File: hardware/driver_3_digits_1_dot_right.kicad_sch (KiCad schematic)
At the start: 11 parts, among them U4 HV5622PG

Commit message: Update.
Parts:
- removed C10: 100nF, Capacitor_SMD:C_1206_3216Metric, symbol Device:C
- removed C9: 0.1uF, Capacitor_SMD:C_1206_3216Metric, symbol Device:C
- removed DOT1: IN-3, nixies-us:nixies-us-IN-3, symbol nixies-us:IN-3
- removed N1, N2, N3: IN-14, nixies-us:nixies-us-IN-14, symbol nixies-us:IN-14
- removed R6, R7, R8: 27K, Resistor_SMD:R_1206_3216Metric, symbol Device:R
- removed R9: 120K, Resistor_SMD:R_1206_3216Metric, symbol Device:R
- removed U4: HV5622PG, Package_QFP:PQFP-44_10x10mm_P0.8mm, symbol HV5622:HV5622PG
- added C13: 0.1uF, Capacitor_SMD:C_1206_3216Metric, symbol Device:C
- added C14: 100nF, Capacitor_SMD:C_1206_3216Metric, symbol Device:C
- added DOT2: IN-3, nixies-us:nixies-us-IN-3, symbol nixies-us:IN-3
- added N4, N5, N6: IN-14, nixies-us:nixies-us-IN-14, symbol nixies-us:IN-14
- added R15, R16, R17: 27K, Resistor_SMD:R_1206_3216Metric, symbol Device:R
- added R18: 120K, Resistor_SMD:R_1206_3216Metric, symbol Device:R
- added U5: HV5622PG, Package_QFP:PQFP-44_10x10mm_P0.8mm, symbol HV5622:HV5622PG
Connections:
- net 12V: now also C13.2, U5.30 (VDD)
- net 170V: now also C14.1, R15.1, R16.1, R17.1, R18.2
- net GND: now also C13.1, C14.2, U5.27 (~{POL}), U5.29 (VSS)
- net NOT_BL: now also U5.33 (~{BL})
- net NOT_LE: now also U5.31 (~{LE})
- net SPI_CLK: now also U5.28 (CLK)
- net SPI_SDI: now also U5.32 (DATA_IN)
- net SPI_SDO: now also U5.23 (DATA_OUT)
- new net: N4.A, R17.2
- new net: DOT2.A, R18.1
- new net: DOT2.K, U5.11 (HVOUT12)
- new net: N5.A, R16.2
- new net: N6.A, R15.2
- new net: N5.0, U5.10 (HVOUT13)
- new net: N5.1, U5.1 (HVOUT22)
- new net: N5.2, U5.2 (HVOUT21)
- new net: N5.3, U5.3 (HVOUT20)
- new net: N5.4, U5.4 (HVOUT19)
- new net: N5.5, U5.5 (HVOUT18)
- new net: N5.6, U5.6 (HVOUT17)
- new net: N5.7, U5.7 (HVOUT16)
- new net: N5.8, U5.8 (HVOUT15)
- new net: N5.9, U5.9 (HVOUT14)
- new net: N6.0, U5.21 (HVOUT2)
- new net: N6.1, U5.12 (HVOUT11)
- new net: N6.2, U5.13 (HVOUT10)
- new net: N6.3, U5.14 (HVOUT9)
- new net: N6.4, U5.15 (HVOUT8)
- new net: N6.5, U5.16 (HVOUT7)
- new net: N6.6, U5.17 (HVOUT6)
- new net: N6.7, U5.18 (HVOUT5)
- new net: N6.8, U5.19 (HVOUT4)
- new net: N6.9, U5.20 (HVOUT3)
- new net: N6.RHDP, U5.22 (HVOUT1)
- new net: N4.0, U5.44 (HVOUT23)
- new net: N4.1, U5.35 (HVOUT32)
- new net: N4.2, U5.36 (HVOUT31)
- new net: N4.3, U5.37 (HVOUT30)
- new net: N4.4, U5.38 (HVOUT29)
- new net: N4.5, U5.39 (HVOUT28)
- new net: N4.6, U5.40 (HVOUT27)
- new net: N4.7, U5.41 (HVOUT26)
- new net: N4.8, U5.42 (HVOUT25)
- new net: N4.9, U5.43 (HVOUT24)
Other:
- title: Nixie driver for three IN-14 and one IN-3 tube -> (none)

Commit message: Update.
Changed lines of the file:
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@@
 		(dnp no)
 		(property "Reference" "N4"
-			(at 121.92 105.918 0)
+			(at 121.92 146.558 0)
 			(effects
 				(font

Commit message: First routage.
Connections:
- net at DOT2.K: now also U5.1 (HVOUT22); no longer U5.11 (HVOUT12)
- net at N5.0: now also U5.11 (HVOUT12); no longer U5.10 (HVOUT13)
- net at N5.1: now also U5.2 (HVOUT21); no longer U5.1 (HVOUT22)
- net at N5.2: now also U5.3 (HVOUT20); no longer U5.2 (HVOUT21)
- net at N5.3: now also U5.4 (HVOUT19); no longer U5.3 (HVOUT20)
- net at N5.4: now also U5.5 (HVOUT18); no longer U5.4 (HVOUT19)
- net at N5.5: now also U5.6 (HVOUT17); no longer U5.5 (HVOUT18)
- net at N5.6: now also U5.7 (HVOUT16); no longer U5.6 (HVOUT17)
- net at N5.7: now also U5.8 (HVOUT15); no longer U5.7 (HVOUT16)
- net at N5.8: now also U5.9 (HVOUT14); no longer U5.8 (HVOUT15)
- net at N5.9: now also U5.10 (HVOUT13); no longer U5.9 (HVOUT14)
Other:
- moved on the sheet: N5

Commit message: Add HT psu.
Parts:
- renumbered N5 to N4, N6 to N5, N4 to N6, R15 to R17, R16 to R18, R17 to R19, R18 to R20
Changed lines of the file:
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@@
 		(dnp no)
 		(fields_autoplaced yes)
-		(property "Reference" "R17"
+		(property "Reference" "R19"
 			(at 138.43 121.92 90)
 			(effects
@@
 			(project "nixie_clock"
 				(path "/90430e5f-7049-4de8-b92d-f897c4a89819/fe830805-1f17-45c2-a3b2-c398af349661"
-					(reference "R17")
+					(reference "R19")
 					(unit 1)
 				)
@@
 		(dnp no)
 		(fields_autoplaced yes)
-		(property "Reference" "R16"
+		(property "Reference" "R18"
 			(at 138.43 39.37 90)
 			(effects
@@
 			(project "nixie_clock"
 				(path "/90430e5f-7049-4de8-b92d-f897c4a89819/fe830805-1f17-45c2-a3b2-c398af349661"
-					(reference "R16")
+					(reference "R18")
 					(unit 1)
 				)
@@
 		(dnp no)
 		(fields_autoplaced yes)
-		(property "Reference" "R15"
+		(property "Reference" "R17"
 			(at 137.16 82.55 90)
 			(effects
@@
 			(project "nixie_clock"
 				(path "/90430e5f-7049-4de8-b92d-f897c4a89819/fe830805-1f17-45c2-a3b2-c398af349661"
-					(reference "R15")
+					(reference "R17")
 					(unit 1)
 				)
@@
 		(on_board yes)
 		(dnp no)
-		(property "Reference" "N5"
+		(property "Reference" "N4"
 			(at 120.65 26.67 0)
 			(effects
@@
 			(project "nixie_clock"
 				(path "/90430e5f-7049-4de8-b92d-f897c4a89819/fe830805-1f17-45c2-a3b2-c398af349661"
-					(reference "N5")
+					(reference "N4")
 					(unit 1)
 				)
@@
 		(on_board yes)
 		(dnp no)
-		(property "Reference" "N6"
+		(property "Reference" "N5"
 			(at 120.65 107.696 0)
 			(effects
@@
 			(project "nixie_clock"
 				(path "/90430e5f-7049-4de8-b92d-f897c4a89819/fe830805-1f17-45c2-a3b2-c398af349661"
-					(reference "N6")
+					(reference "N5")
 					(unit 1)
 				)
@@
 		(on_board yes)
 		(dnp no)
-		(property "Reference" "N4"
+		(property "Reference" "N6"
 			(at 121.92 146.558 0)
 			(effects
@@
 			(project "nixie_clock"
 				(path "/90430e5f-7049-4de8-b92d-f897c4a89819/fe830805-1f17-45c2-a3b2-c398af349661"
-					(reference "N4")
+					(reference "N6")
 					(unit 1)
 				)
@@
 		(dnp no)
 		(fields_autoplaced yes)
-		(property "Reference" "R18"
+		(property "Reference" "R20"
 			(at 170.18 55.88 90)
 			(effects
@@
 			(project "nixie_clock"
 				(path "/90430e5f-7049-4de8-b92d-f897c4a89819/fe830805-1f17-45c2-a3b2-c398af349661"
-					(reference "R18")
+					(reference "R20")
 					(unit 1)
 				)

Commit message: Rename nixie's names to have the right order.
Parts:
- renumbered N6 to N4, N4 to N5, N5 to N6
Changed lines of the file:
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@@
 		(on_board yes)
 		(dnp no)
-		(property "Reference" "N4"
+		(property "Reference" "N5"
 			(at 120.65 26.67 0)
 			(effects
@@
 			(project "nixie_clock"
 				(path "/90430e5f-7049-4de8-b92d-f897c4a89819/fe830805-1f17-45c2-a3b2-c398af349661"
-					(reference "N4")
+					(reference "N5")
 					(unit 1)
 				)
@@
 		(on_board yes)
 		(dnp no)
-		(property "Reference" "N5"
+		(property "Reference" "N6"
 			(at 120.65 107.696 0)
 			(effects
@@
 			(project "nixie_clock"
 				(path "/90430e5f-7049-4de8-b92d-f897c4a89819/fe830805-1f17-45c2-a3b2-c398af349661"
-					(reference "N5")
+					(reference "N6")
 					(unit 1)
 				)
@@
 		(on_board yes)
 		(dnp no)
-		(property "Reference" "N6"
+		(property "Reference" "N4"
 			(at 121.92 146.558 0)
 			(effects
@@
 			(project "nixie_clock"
 				(path "/90430e5f-7049-4de8-b92d-f897c4a89819/fe830805-1f17-45c2-a3b2-c398af349661"
-					(reference "N6")
+					(reference "N4")
 					(unit 1)
 				)

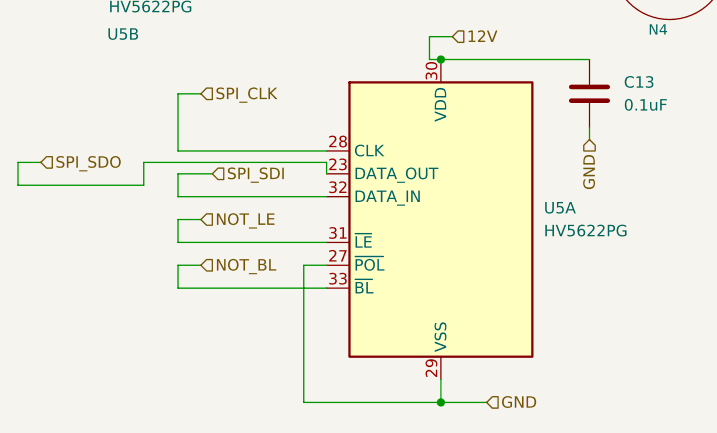
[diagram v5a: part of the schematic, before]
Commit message: Remove POLarity setup, needs 12V to be not reversed.
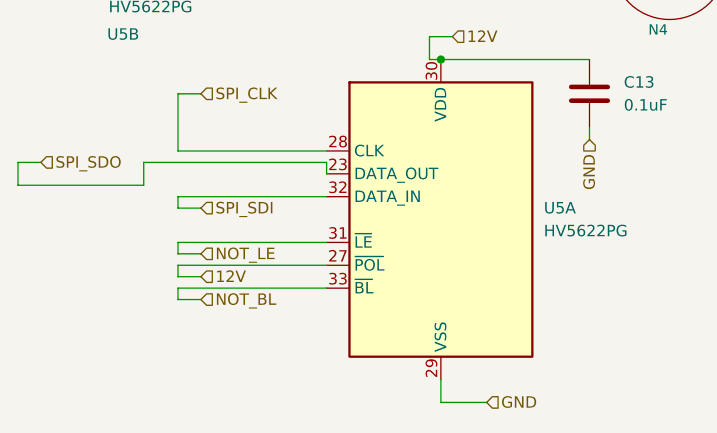
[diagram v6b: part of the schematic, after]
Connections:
- net 12V: now also U5.27 (~{POL})
- net GND: no longer U5.27 (~{POL})

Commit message: C15, C13, C9  changed to 805 form factor. Removed tracks under capacitors.
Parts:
- C13: footprint Capacitor_SMD:C_1206_3216Metric -> Resistor_SMD:R_0805_2012Metric
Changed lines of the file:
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@@
 			)
 		)
-		(property "Footprint" "Capacitor_SMD:C_1206_3216Metric"
+		(property "Footprint" "Resistor_SMD:R_0805_2012Metric"
 			(at 113.3348 149.86 0)
 			(effects

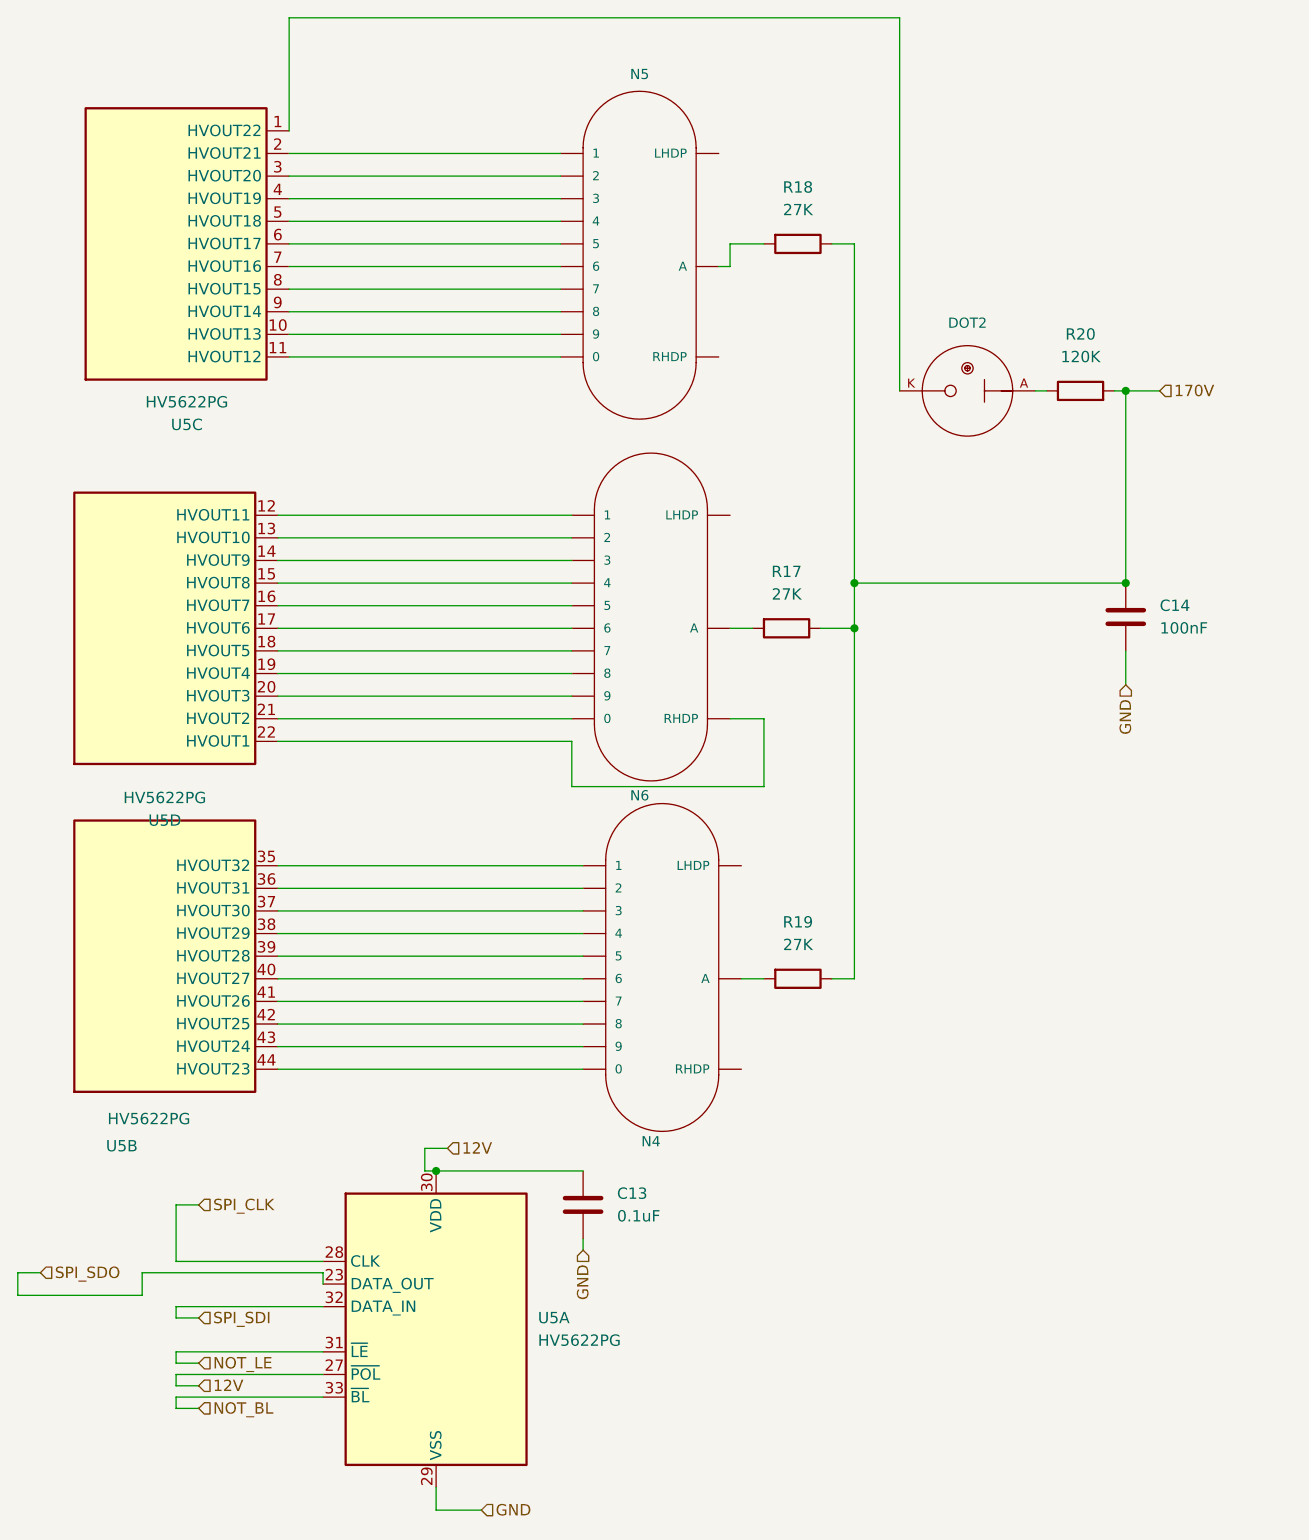
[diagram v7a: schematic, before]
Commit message: Rework  3.3v power supply (fix error on fb loop). Put 1206 back on HV part.
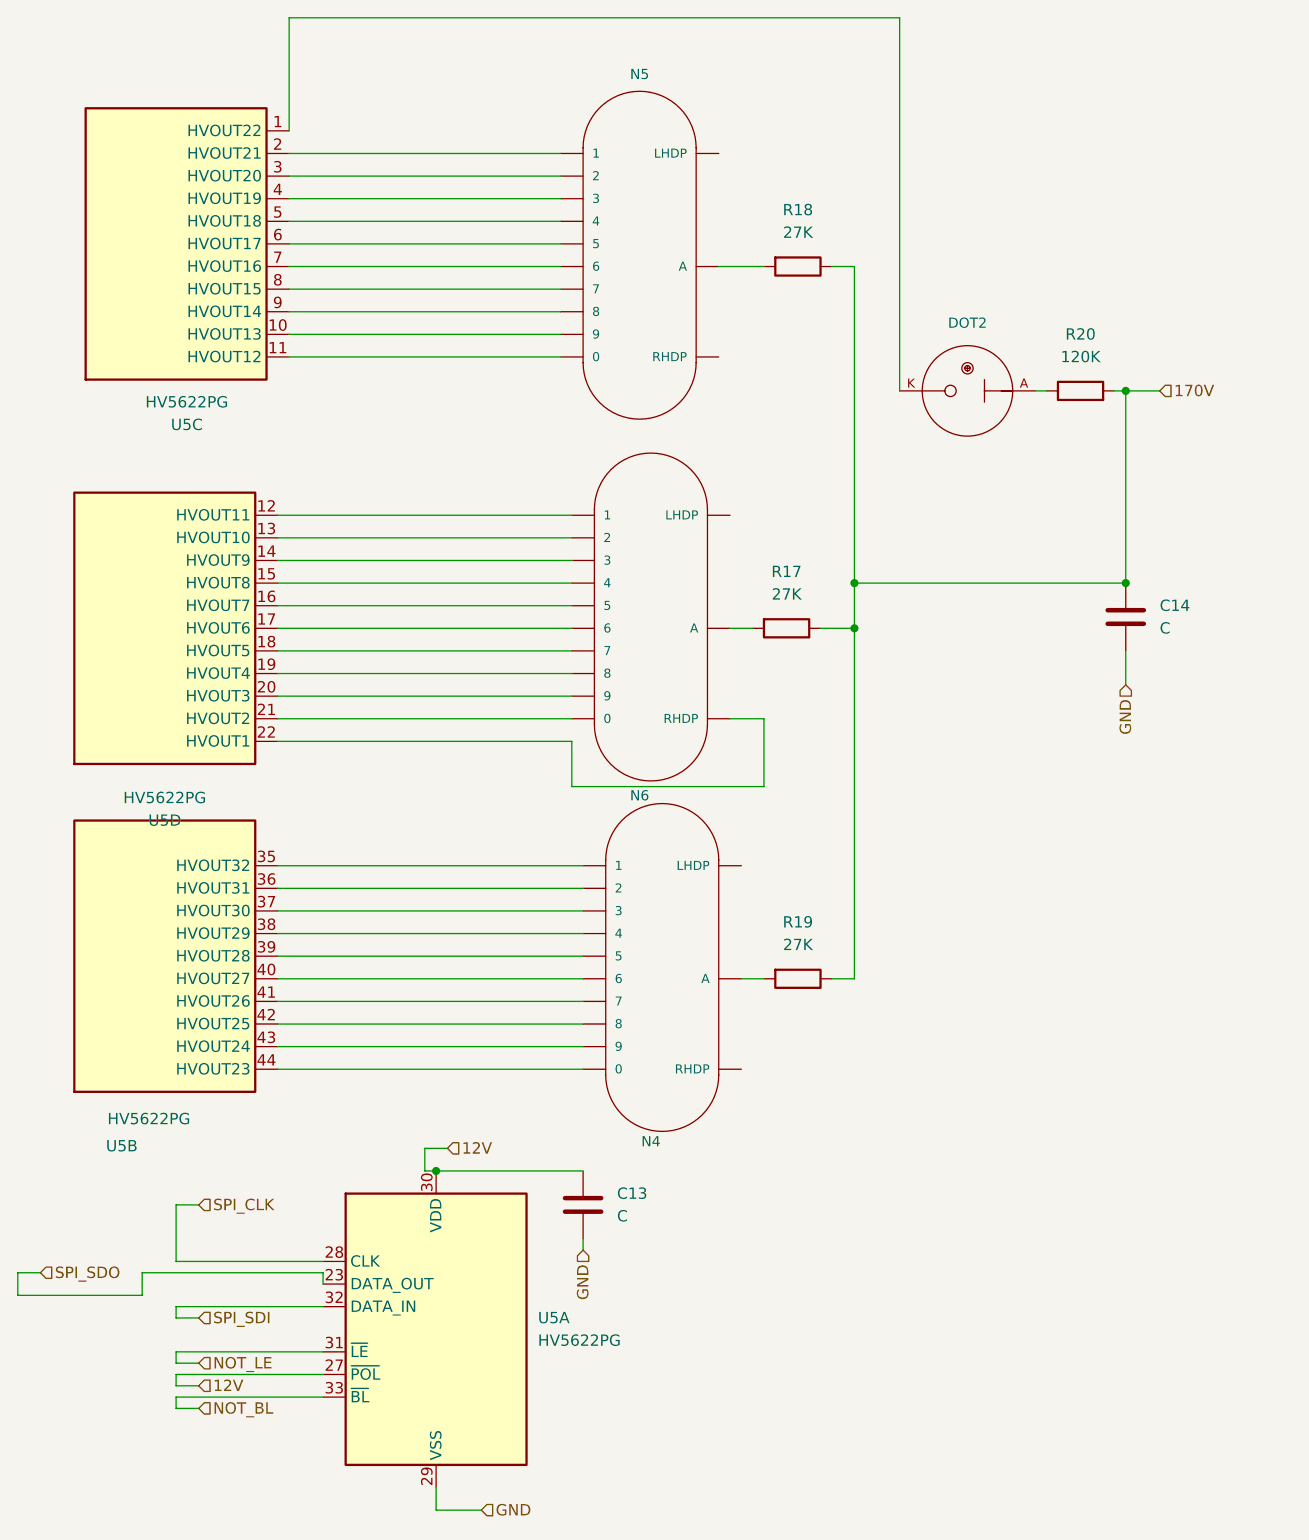
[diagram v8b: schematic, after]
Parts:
- C13: value 0.1uF -> C
- C14: value 100nF -> C
- DOT2: footprint nixies-us:nixies-us-IN-3 -> nixies-us_IN-3
- N4, N5, N6: footprint nixies-us:nixies-us-IN-14 -> nixies-us_IN-14
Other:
- moved on the sheet: R18
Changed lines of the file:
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@@
-	(wire
-		(pts
-			(xy 130.81 45.72) (xy 134.62 45.72)
-		)
-		(stroke
-			(width 0)
-			(type default)
-		)
-	)
 	(wire
 		(pts
@@
 	(wire
 		(pts
-			(xy 130.81 48.26) (xy 130.81 45.72)
-		)
-		(stroke
-			(width 0)
-			(type default)
-		)
-	)
-	(wire
-		(pts
 			(xy 64.77 161.29) (xy 64.77 163.83)
 		)
@@
 	(wire
 		(pts
-			(xy 129.54 48.26) (xy 130.81 48.26)
+			(xy 129.54 48.26) (xy 134.62 48.26)
 		)
 		(stroke
@@
 	(wire
 		(pts
-			(xy 144.78 45.72) (xy 144.78 83.82)
+			(xy 144.78 48.26) (xy 144.78 83.82)
 		)
 		(stroke
@@
 	(wire
 		(pts
-			(xy 142.24 45.72) (xy 144.78 45.72)
+			(xy 142.24 48.26) (xy 144.78 48.26)
 		)
 		(stroke
@@
 			)
 		)
-		(property "Value" "0.1uF"
+		(property "Value" "C"
 			(at 118.11 154.9399 0)
 			(effects
@@
 			)
 		)
-		(property "Footprint" "nixies-us:nixies-us-IN-3"
+		(property "Footprint" "nixies-us_IN-3"
 			(at 161.798 55.88 0)
 			(effects
@@
 	(symbol
 		(lib_id "Device:R")
-		(at 138.43 45.72 270)
+		(at 138.43 48.26 270)
 		(unit 1)
 		(exclude_from_sim no)
@@
 		(fields_autoplaced yes)
 		(property "Reference" "R18"
-			(at 138.43 39.37 90)
+			(at 138.43 41.91 90)
 			(effects
 				(font
@@
 		)
 		(property "Value" "27K"
-			(at 138.43 41.91 90)
+			(at 138.43 44.45 90)
 			(effects
 				(font
@@
 		)
 		(property "Footprint" "Resistor_SMD:R_1206_3216Metric"
-			(at 138.43 43.942 90)
+			(at 138.43 46.482 90)
 			(effects
 				(font
@@
 		)
 		(property "Datasheet" "~"
-			(at 138.43 45.72 0)
+			(at 138.43 48.26 0)
 			(effects
 				(font
@@
 		)
 		(property "Description" "Resistor"
-			(at 138.43 45.72 0)
+			(at 138.43 48.26 0)
 			(effects
 				(font
@@
 			)
 		)
-		(property "Footprint" "nixies-us:nixies-us-IN-14"
+		(property "Footprint" "nixies-us_IN-14"
 			(at 120.142 41.91 0)
 			(effects
@@
 			)
 		)
-		(property "Footprint" "nixies-us:nixies-us-IN-14"
+		(property "Footprint" "nixies-us_IN-14"
 			(at 121.412 82.55 0)
 			(effects
@@
 			)
 		)
-		(property "Footprint" "nixies-us:nixies-us-IN-14"
+		(property "Footprint" "nixies-us_IN-14"
 			(at 122.682 121.92 0)
 			(effects
@@
 			)
 		)
-		(property "Value" "100nF"
+		(property "Value" "C"
 			(at 179.07 88.8999 0)
 			(effects
